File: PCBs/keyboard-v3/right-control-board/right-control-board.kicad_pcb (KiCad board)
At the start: 2 copper layers, 111.9 x 40 mm, 67 parts, among them J101 USB4510-03-1-A, J102 USB4510-03-1-A, J103 GSB12J21C1EU, J201 USB4510-03-1-A, J501 Conn_02x08_Odd_Even, J601 F31Z1A7H111008, J602 F31Z1A7H111008, J701 Conn_01x02, U101 USB2534-1080AEN, U104 USBLC6-4SC6, U201 USBLC6-4SC6, U401 NINA-B302-00B, U601 NCP380HMU05AATBG, U602 NCP380HMU05AATBG, U701 TPS62290TDRVRQ1, U702 BQ25185DLHR, U801 NCP380HMU05AATBG, Y101 CX2016SA24000D0HLLG3

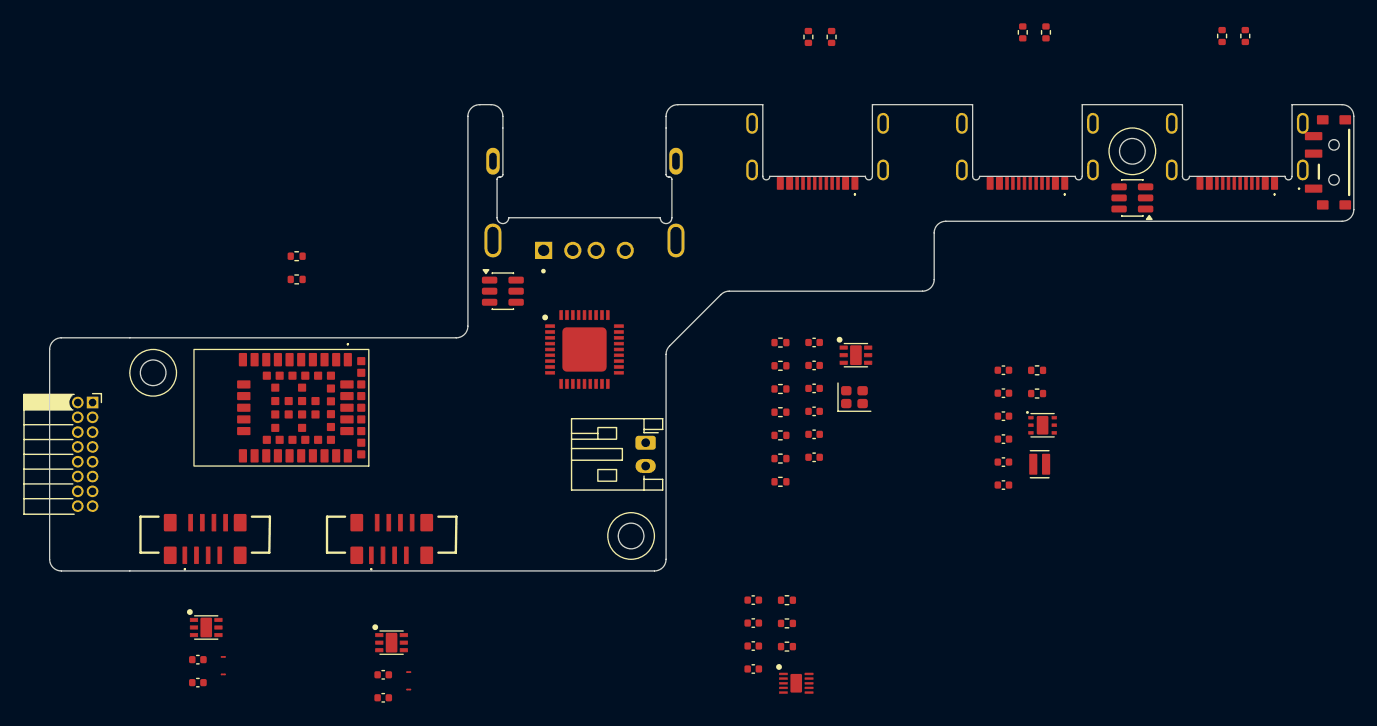
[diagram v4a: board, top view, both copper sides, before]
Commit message: Right control board placement and schematic done
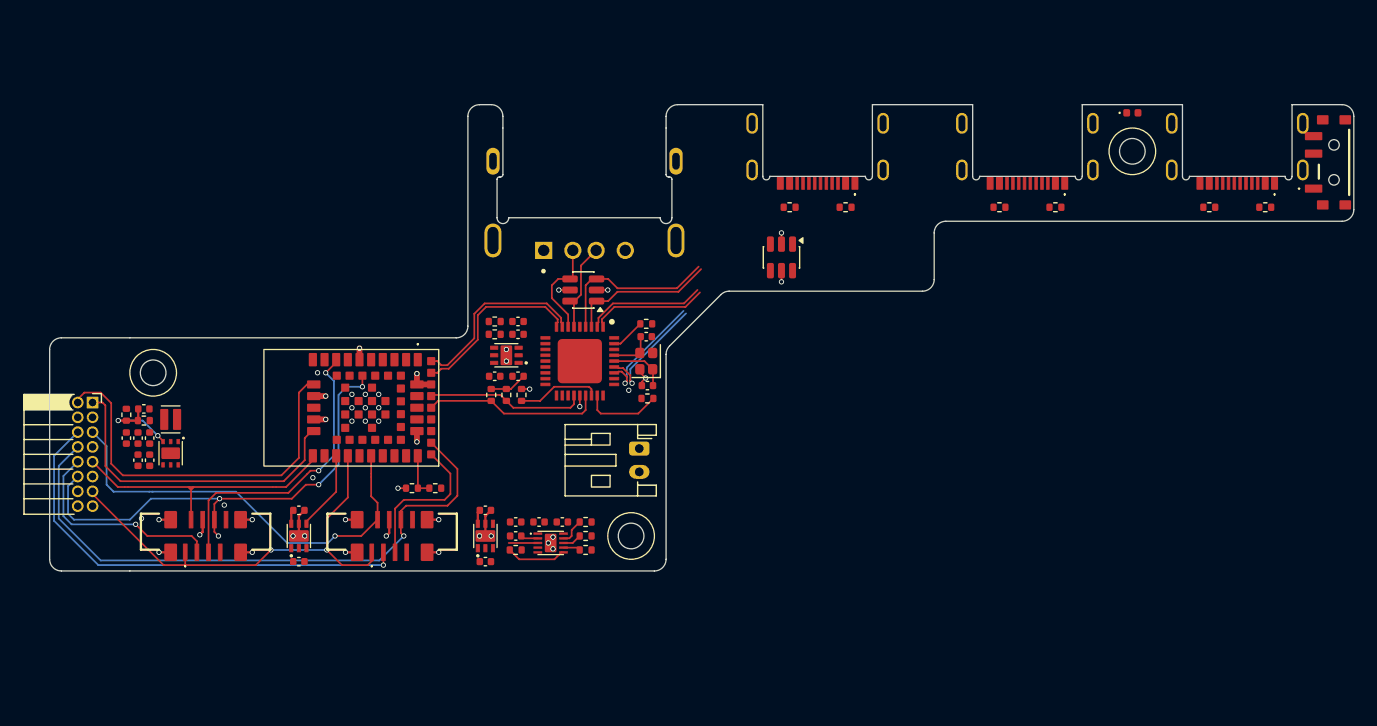
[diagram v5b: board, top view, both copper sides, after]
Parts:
- added D701: RED, project_footprints:LED_0402, F.Cu at (187.0, 78.7)
- added R706: 10k, project_footprints:R_0402, F.Cu at (140.1, 113.8)
- NT601: moved to B.Cu
- R701: value 820k -> 806k
- R702: value 182k -> 180k
- moved R702 78.2 mm to (100.7, 104.6), turned to 90 degrees
- moved R701 76.8 mm to (102.2, 105.1), turned to 180 degrees
- moved C206 75.3 mm to (100.7, 106.6), turned to -90 degrees
- moved U701 74.8 mm to (104.5, 107.9), turned to -90 degrees
- moved L201 74.6 mm to (104.5, 105.0), turned to 180 degrees
- moved C202 74.5 mm to (101.7, 108.5), turned to 90 degrees
- moved C205 74.3 mm to (101.7, 106.6), turned to -90 degrees
- moved C203 73.7 mm to (102.2, 104.1), turned to 180 degrees
- moved C201 73.6 mm to (102.7, 108.5), turned to 90 degrees
- moved C204 73.2 mm to (102.7, 106.6), turned to -90 degrees
- moved U104 30.5 mm to (156.9, 91.1), turned to -90 degrees
- moved U801 30.0 mm to (133.3, 99.5), turned to 180 degrees
- moved C801 28.3 mm to (132.3, 101.3)
- moved C106 27.2 mm to (134.3, 96.6), turned to 180 degrees
- moved NT601 27.0 mm to (102.8, 111.2)
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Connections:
- net /Power/FB_1V8 renamed /Power/FB_3V3
- net /Power/SW_1V8 renamed /Power/SW_3V3
- net Net-(S701-COM) renamed /Power/EN
- J501 pad 1: /Debug Connector/CTRL.SWCLK -> /Debug Connector/CTRL.SWDIO
- J501 pad 10: /Daughter Board Connectors/KEYS.SWDIO -> /Daughter Board Connectors/KEYS.SWCLK
- J501 pad 12: /Debug Connector/KEYS.RX -> /Daughter Board Connectors/KEYS.RX
- J501 pad 2: /Debug Connector/CTRL.SWDIO -> /Debug Connector/CTRL.SWCLK
- J501 pad 5: /Daughter Board Connectors/KNOB.SWCLK -> /Daughter Board Connectors/KNOB.SWDIO
- J501 pad 6: /Daughter Board Connectors/KNOB.SWDIO -> /Daughter Board Connectors/KNOB.SWCLK
- J501 pad 8: /Debug Connector/KNOB.RX -> /Daughter Board Connectors/KNOB.RX
- J501 pad 9: /Daughter Board Connectors/KEYS.SWCLK -> /Daughter Board Connectors/KEYS.SWDIO
- U201 pad 1: /USB Connectors/USB2.DP -> /USB Connectors/USB2.DN
- U201 pad 3: /USB Connectors/USB2.DN -> /USB Connectors/USB2.DP
- U401 pad 16: unconnected-(U401-P0.03-Pad16) -> /Daughter Board Connectors/~{KEYS_INT}
- U401 pad 18: unconnected-(U401-P0.02-Pad18) -> /Daughter Board Connectors/KEYS_5V_EN
- U401 pad 21: unconnected-(U401-P1.12-Pad21) -> /Daughter Board Connectors/~{KNOB_INT}
- U401 pad 34: unconnected-(U401-P1.08-Pad34) -> /Daughter Board Connectors/KEYS.RX
- U401 pad 47: unconnected-(U401-P0.23/QSPI_D3-Pad47) -> /Daughter Board Connectors/KNOB.TX
- U401 pad 48: unconnected-(U401-P0.21/QSPI_D1-Pad48) -> /Daughter Board Connectors/KNOB.RX
- U401 pad 49: unconnected-(U401-P0.22/QSPI_D2-Pad49) -> /Daughter Board Connectors/KNOB_5V_EN
- U401 pad 51: unconnected-(U401-P0.17/QSPI_CS-Pad51) -> /MCU/SCL
- U401 pad 52: unconnected-(U401-P0.19/QSPI_CLK-Pad52) -> /MCU/SDA
- U401 pad 8: unconnected-(U401-P1.00/SWO/TRACE_D0-Pad8) -> /Daughter Board Connectors/KEYS.TX
- U702 pad 3: /Power/CHG_STAT2 -> /Power/STAT2
- U702 pad 9: /Power/CHG_STAT1 -> /Power/STAT1
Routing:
- net /Daughter Board Connectors/KNOB.RX: track 0.00 -> 51.9 mm, vias 0 -> 1
- net /Daughter Board Connectors/KEYS.RX: track 0.00 -> 41.7 mm, vias 0 -> 4
- net /Daughter Board Connectors/KNOB.SWCLK: track 0.00 -> 39.4 mm, vias 0 -> 1
- net /Daughter Board Connectors/~{KEYS_RST}: track 0.00 -> 38.6 mm, vias 0 -> 2
- net /Debug Connector/CTRL.SWCLK: track 0.00 -> 33.3 mm
- net /Debug Connector/CTRL.SWDIO: track 0.00 -> 27.7 mm
- net GND: track 0.00 -> 26.9 mm, vias 0 -> 43
- net /Daughter Board Connectors/KNOB_SWDIO/~{KNOB_INT}: track 0.00 -> 25.8 mm, vias 0 -> 1
- net /Daughter Board Connectors/KEYS.TX: track 0.00 -> 25.7 mm, vias 0 -> 2
- net /Daughter Board Connectors/KEYS.SWCLK: track 0.00 -> 18.5 mm, vias 0 -> 1
- net /MCU/DN: track 0.00 -> 16.0 mm
- net /MCU/DP: track 0.00 -> 15.5 mm
- net /MCU/SCL: track 0.00 -> 15.3 mm
- net /Daughter Board Connectors/KEYS_SWDIO/~{INT}: track 0.00 -> 15.2 mm
- net /USB Connectors/USB2.DP: track 0.00 -> 14.7 mm
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- added copper zone on In1.Cu, net GND
- added copper zone on In2.Cu, net GND
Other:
- copper layers 2 -> 4

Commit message: Right control board ~50 unrouted
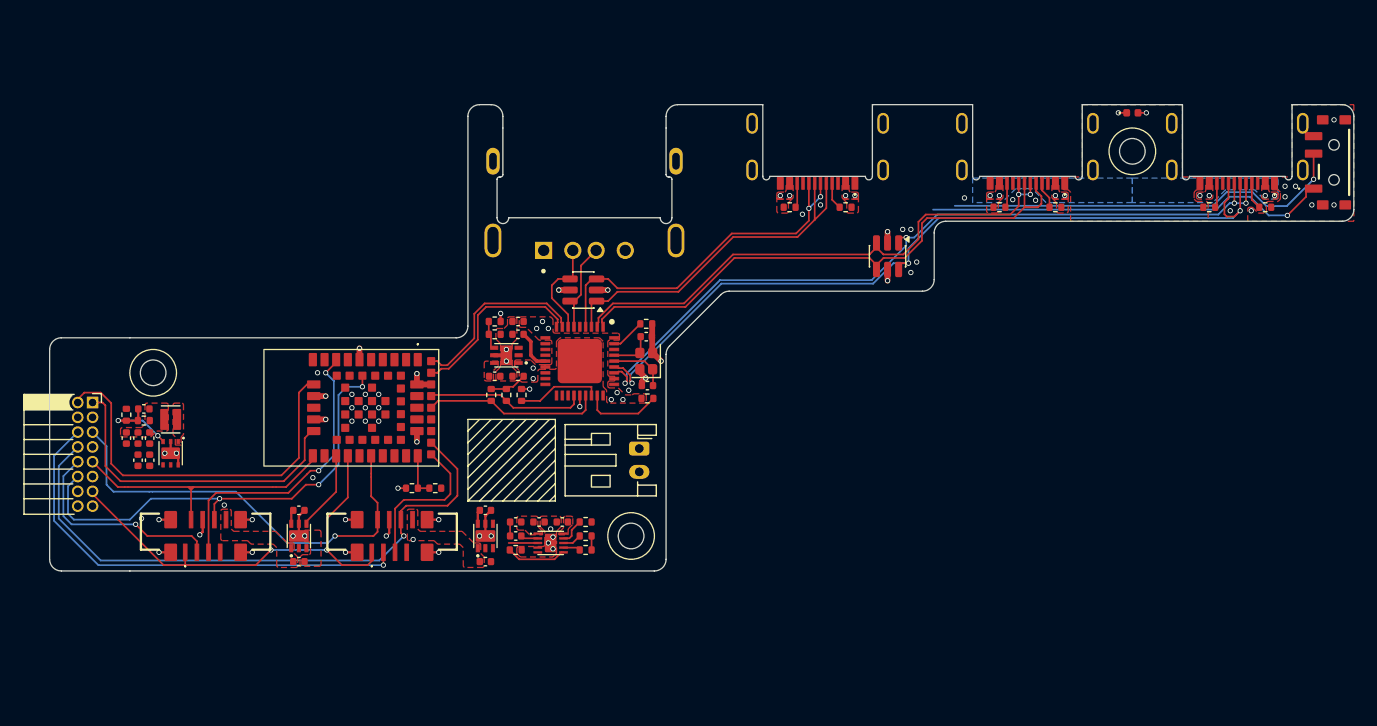
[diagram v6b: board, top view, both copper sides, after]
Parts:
- moved U104 9.10 mm to (166.0, 91.0)
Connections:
- U104 pad 1: /USB Connectors/USB0.DP -> /USB Connectors/USB0.DN
- U104 pad 3: /USB Connectors/USB0.DN -> /USB Connectors/USB1.DP
- U104 pad 4: /USB Connectors/USB1.DP -> /USB Connectors/USB1.DN
- U104 pad 6: /USB Connectors/USB1.DN -> /USB Connectors/USB0.DP
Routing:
- net /USB Connectors/USB0.DP: track 10.5 -> 69.7 mm, vias 1 -> 3
- net /USB Connectors/USB0.DN: track 10.2 -> 66.5 mm, vias 1 -> 4
- net /USB Connectors/USB1.DN: track 10.0 -> 48.2 mm
- net /USB Connectors/USB1.DP: track 10.3 -> 46.5 mm, vias 0 -> 2
- net /Power/EN: track 0.00 -> 34.9 mm, vias 0 -> 1
- net +VSYS: track 2.44 -> 36.9 mm, vias 0 -> 1
- net /Power/STAT1: track 2.27 -> 24.4 mm, vias 0 -> 1
- net /Power/STAT2: track 2.50 -> 22.2 mm, vias 0 -> 1
- net /USB Connectors/USB2.DN: track 12.3 -> 30.5 mm
- net /USB Connectors/USB2.DP: track 14.7 -> 31.5 mm, vias 0 -> 2
- net GND: track 26.9 -> 35.9 mm, vias 43 -> 65
- net +1V2: track 0.00 -> 3.51 mm
- net /USB Connectors/USB2_CC1: track 0.00 -> 2.32 mm
- net /USB Connectors/USB1_CC1: track 0.00 -> 2.32 mm
- net /USB Connectors/USB0_CC1: track 0.00 -> 2.32 mm
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- added copper zone on F.Cu, net +3V3
- added copper zone on F.Cu, net +3V3_USB
- added copper zone on F.Cu, net +VSYS
- added copper zone on F.Cu, net /Daughter Board Connectors/KEYS_5V
- added copper zone on F.Cu, net /Daughter Board Connectors/KNOB_5V
- added copper zone on F.Cu, net /Power/SW_3V3
- added copper zone on F.Cu, net GND
- added copper zone on B.Cu, net VBUS
- added copper zone on F.Cu, net VBUS

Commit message: Right control board routing finished
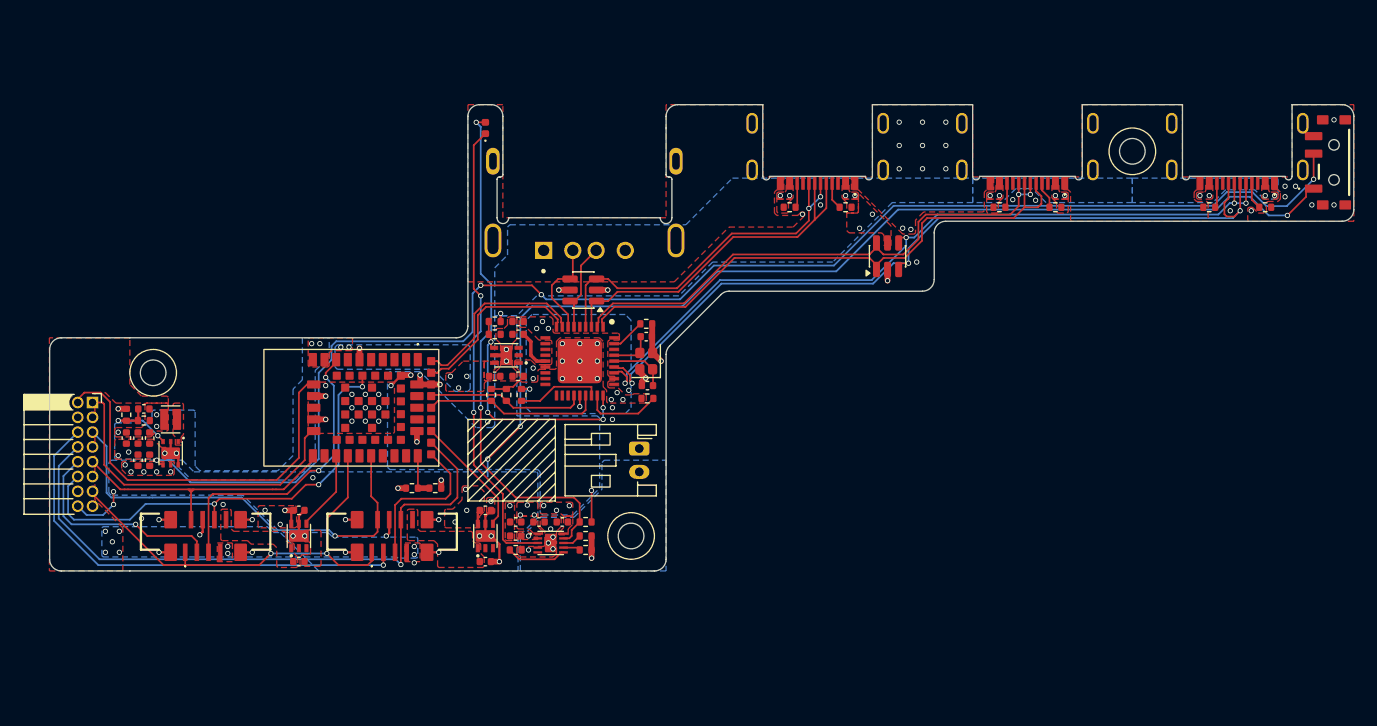
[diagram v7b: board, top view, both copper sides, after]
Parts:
- moved D701 55.5 mm to (131.5, 80.0), turned to 90 degrees
- moved NT601 0.50 mm to (102.8, 111.7)
- moved NT603 0.20 mm to (100.7, 111.0)
- moved NT604 0.20 mm to (113.4, 111.0)
- turned U104 to 90 degrees
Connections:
- J501 pad 16: VBUS -> +VSYS
- U104 pad 1: /USB Connectors/USB0.DN -> /USB Connectors/USB1.DN
- U104 pad 3: /USB Connectors/USB1.DP -> /USB Connectors/USB0.DP
- U104 pad 4: /USB Connectors/USB1.DN -> /USB Connectors/USB0.DN
- U104 pad 6: /USB Connectors/USB0.DP -> /USB Connectors/USB1.DP
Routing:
- net /Power/EN: track 34.9 -> 122.7 mm, vias 1 -> 4
- net +VSYS: track 36.9 -> 97.2 mm, vias 1 -> 20
- net /Power/STAT1: track 24.4 -> 44.7 mm, vias 1 -> 2
- net /USB Hub/VBUS_DET: track 2.04 -> 20.4 mm, vias 0 -> 4
- net /Power/STAT2: track 22.2 -> 39.9 mm, vias 1 -> 2
- net /Daughter Board Connectors/KNOB_5V_EN: track 0.00 -> 10.5 mm
- net VBUS: track 2.61 -> 6.43 mm, vias 15 -> 22
- net GND: track 35.9 -> 39.7 mm, vias 65 -> 93
- net /Daughter Board Connectors/KNOB.RX: track 51.9 -> 53.5 mm
- net /Power/BAT: track 1.50 -> 0.00 mm, vias 0 -> 1
- net /Daughter Board Connectors/KNOB_SWDIO/~{KNOB_INT}: track 26.4 -> 25.7 mm
- net /Daughter Board Connectors/KEYS.RX: track 40.2 -> 39.5 mm
- net /Daughter Board Connectors/KNOB.SWDIO: track 8.92 -> 9.54 mm
- net +3V3: vias 0 -> 19
- added copper zone on B.Cu, net +3V3
- added copper zone on B.Cu, net +3V3_USB
- added copper zone on B.Cu, net +VSYS
- added copper zone on B.Cu, net /Power/BAT
- added copper zone on F.Cu, net /Power/BAT

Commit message: Added mounting holes
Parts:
- renumbered C604 to C602, C602 to C603, C603 to C604, C703 to C701, C701 to C702, C702 to C703, C201 to C705, C202 to C706, C203 to C707, C204 to C708, C205 to C709, C206 to C710, C105 to C801, C106 to C802, C801 to C803, C101 to C804, C102 to C805, C103 to C806, J101 to J201, J102 to J202, J201 to J203, J103 to J204, L201 to L701, R203 to R201, R208 to R202, R209 to R203, R210 to R204, R402 to R401, R401 to R402, R706 to R701, R703 to R702, R704 to R703, R705 to R704, R701 to R705, R702 to R706, R105 to R801, R104 to R802, R102 to R803, R101 to R804, R103 to R805, R108 to R806, R801 to R807, U104 to U201, U201 to U202, U702 to U701, U701 to U702, U101 to U802, Y101 to Y801
